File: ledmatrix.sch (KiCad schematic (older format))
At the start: 4 parts

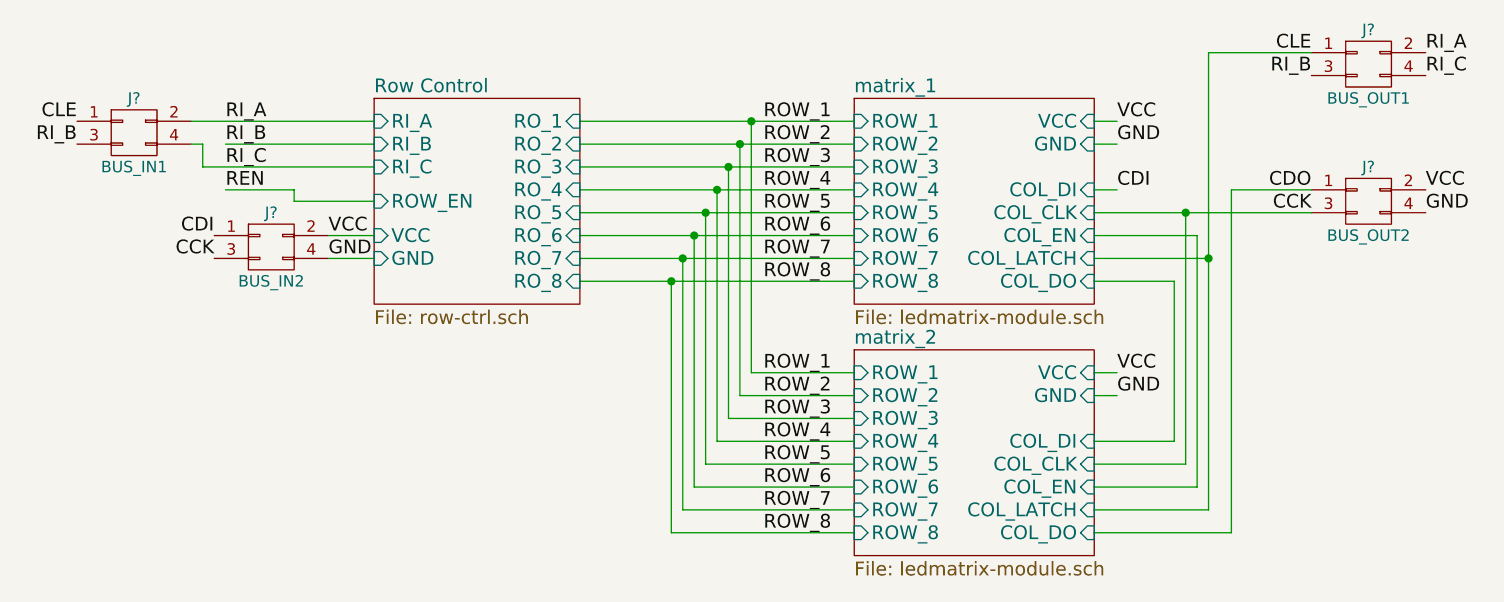
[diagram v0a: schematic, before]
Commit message: fix matrix module order
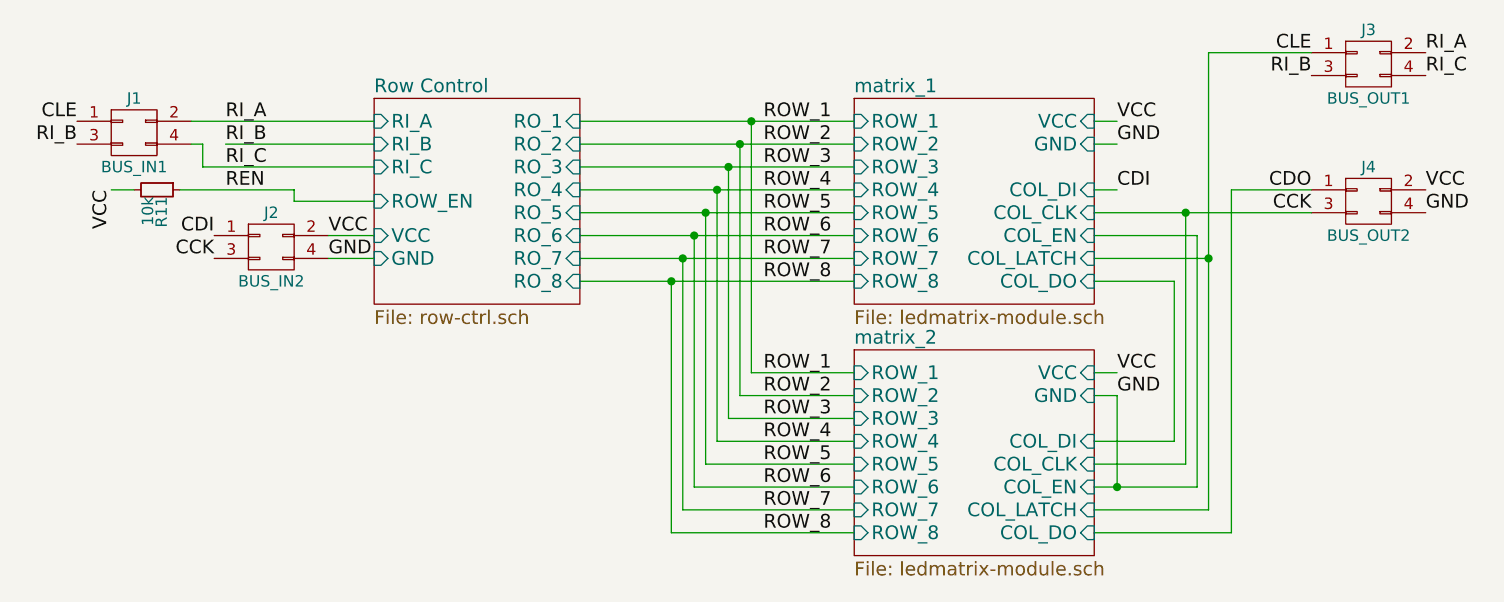
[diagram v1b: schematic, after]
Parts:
- added R11: 10k, symbol R_Small
- gave numbers to parts that had none: 4
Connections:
- net REN: now also R11.1
- net VCC: now also R11.2
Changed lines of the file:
@@
 REN
 Wire Wire Line
-	2250 1800 2550 1800
+	2050 1800 2550 1800
 Wire Wire Line
 	2550 1800 2550 1850
@@
 	6450 3000 6450 1900
 $Comp
-L CONN_02X02 J?
+L CONN_02X02 J4
 U 1 1 59AB19E8
 P 7250 1850
-F 0 "J?" H 7250 2000 50  0000 C CNN
+F 0 "J4" H 7250 2000 50  0000 C CNN
 F 1 "BUS_OUT2" H 7250 1700 50  0000 C CNN
 F 2 "" H 7250 650 50  0001 C CNN
@@
 	6500 2000 6050 2000
 $Comp
-L CONN_02X02 J?
+L CONN_02X02 J3
 U 1 1 59AB23F4
 P 7250 1250
-F 0 "J?" H 7250 1400 50  0000 C CNN
+F 0 "J3" H 7250 1400 50  0000 C CNN
 F 1 "BUS_OUT1" H 7250 1100 50  0000 C CNN
 F 2 "" H 7250 50  50  0001 C CNN
@@
 CLE
 $Comp
-L CONN_02X02 J?
+L CONN_02X02 J2
 U 1 1 59AB4B91
 P 2450 2050
-F 0 "J?" H 2450 2200 50  0000 C CNN
+F 0 "J2" H 2450 2200 50  0000 C CNN
 F 1 "BUS_IN2" H 2450 1900 50  0000 C CNN
 F 2 "" H 2450 850 50  0001 C CNN
@@
 $EndComp
 $Comp
-L CONN_02X02 J?
+L CONN_02X02 J1
 U 1 1 59AB4B97
 P 1850 1550
-F 0 "J?" H 1850 1700 50  0000 C CNN
+F 0 "J1" H 1850 1700 50  0000 C CNN
 F 1 "BUS_IN1" H 1850 1400 50  0000 C CNN
 F 2 "" H 1850 350 50  0001 C CNN
@@
 Wire Wire Line
 	2100 1500 2900 1500
+Wire Wire Line
+	6150 2700 6150 3100
+Connection ~ 6150 3100
+$Comp
+L R_Small R11
+U 1 1 59AB4113
+P 1950 1800
+F 0 "R11" H 1980 1820 50  0000 L CNN
+F 1 "10k" H 1980 1760 50  0000 L CNN
+F 2 "" H 1950 1800 50  0001 C CNN
+F 3 "" H 1950 1800 50  0001 C CNN
+	1    1950 1800
+	0    1    1    0
+$EndComp
+Wire Wire Line
+	1850 1800 1750 1800
+Text Label 1750 1800 3    60   ~ 0
+VCC
 $EndSCHEMATC

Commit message: save schematic changes
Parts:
- J1, J2: footprint (none) -> footprints:PINHDR_2x2_angled_male
- J3, J4: footprint (none) -> footprints:PINHDR_2x2_angled_female
- R11: footprint (none) -> footprints:0603_HAND
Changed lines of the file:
@@
 F 0 "J4" H 7250 2000 50  0000 C CNN
 F 1 "BUS_OUT2" H 7250 1700 50  0000 C CNN
-F 2 "" H 7250 650 50  0001 C CNN
+F 2 "footprints:PINHDR_2x2_angled_female" H 7250 650 50  0001 C CNN
 F 3 "" H 7250 650 50  0001 C CNN
 	1    7250 1850
@@
 F 0 "J3" H 7250 1400 50  0000 C CNN
 F 1 "BUS_OUT1" H 7250 1100 50  0000 C CNN
-F 2 "" H 7250 50  50  0001 C CNN
+F 2 "footprints:PINHDR_2x2_angled_female" H 7250 50  50  0001 C CNN
 F 3 "" H 7250 50  50  0001 C CNN
 	1    7250 1250
@@
 F 0 "J2" H 2450 2200 50  0000 C CNN
 F 1 "BUS_IN2" H 2450 1900 50  0000 C CNN
-F 2 "" H 2450 850 50  0001 C CNN
+F 2 "footprints:PINHDR_2x2_angled_male" H 2450 850 50  0001 C CNN
 F 3 "" H 2450 850 50  0001 C CNN
 	1    2450 2050
@@
 F 0 "J1" H 1850 1700 50  0000 C CNN
 F 1 "BUS_IN1" H 1850 1400 50  0000 C CNN
-F 2 "" H 1850 350 50  0001 C CNN
+F 2 "footprints:PINHDR_2x2_angled_male" H 1850 350 50  0001 C CNN
 F 3 "" H 1850 350 50  0001 C CNN
 	1    1850 1550
@@
 F 0 "R11" H 1980 1820 50  0000 L CNN
 F 1 "10k" H 1980 1760 50  0000 L CNN
-F 2 "" H 1950 1800 50  0001 C CNN
+F 2 "footprints:0603_HAND" H 1950 1800 50  0001 C CNN
 F 3 "" H 1950 1800 50  0001 C CNN
 	1    1950 1800

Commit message: add bypassing to schematic
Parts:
- added C1: 10u, footprints:0805_HAND, symbol C_Small
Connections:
- net GND: now also C1.2
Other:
- moved on the sheet: J2
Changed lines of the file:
@@
 Text Label 1600 1600 2    60   ~ 0
 RI_B
-Text Label 2200 2100 2    60   ~ 0
+Text Label 1650 2400 2    60   ~ 0
 CCK
 Text Label 1600 1500 2    60   ~ 0
@@
 L CONN_02X02 J2
 U 1 1 59AB4B91
-P 2450 2050
-F 0 "J2" H 2450 2200 50  0000 C CNN
-F 1 "BUS_IN2" H 2450 1900 50  0000 C CNN
-F 2 "footprints:PINHDR_2x2_angled_male" H 2450 850 50  0001 C CNN
-F 3 "" H 2450 850 50  0001 C CNN
-	1    2450 2050
+P 1900 2350
+F 0 "J2" H 1900 2500 50  0000 C CNN
+F 1 "BUS_IN2" H 1900 2200 50  0000 C CNN
+F 2 "footprints:PINHDR_2x2_angled_male" H 1900 1150 50  0001 C CNN
+F 3 "" H 1900 1150 50  0001 C CNN
+	1    1900 2350
 	1    0    0    -1
 $EndComp
@@
 VCC
 Wire Wire Line
-	2700 2000 2900 2000
+	2150 2000 2900 2000
 Wire Wire Line
 	2700 2100 2900 2100
-Text Label 2200 2000 2    60   ~ 0
+Text Label 1650 2300 2    60   ~ 0
 CDI
 Wire Wire Line
@@
 Text Label 1750 1800 3    60   ~ 0
 VCC
+Wire Wire Line
+	2150 2300 2150 2000
+$Comp
+L C_Small C1
+U 1 1 59ABF7FF
+P 2400 2100
+F 0 "C1" H 2410 2170 50  0000 L CNN
+F 1 "10u" H 2410 2020 50  0000 L CNN
+F 2 "footprints:0805_HAND" H 2400 2100 50  0001 C CNN
+F 3 "" H 2400 2100 50  0001 C CNN
+	1    2400 2100
+	1    0    0    -1
+$EndComp
+Wire Wire Line
+	2400 2200 2400 2400
+Wire Wire Line
+	2400 2400 2150 2400
+Text Label 2150 2400 0    60   ~ 0
+GND
 $EndSCHEMATC

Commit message: fully connected PCB
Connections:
- net VCC: now also C1.1
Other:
- moved on the sheet: C1
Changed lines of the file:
@@
 VCC
-Wire Wire Line
-	2150 2000 2900 2000
 Wire Wire Line
 	2700 2100 2900 2100
@@
 Wire Wire Line
 	2150 2300 2150 2000
-$Comp
-L C_Small C1
-U 1 1 59ABF7FF
-P 2400 2100
-F 0 "C1" H 2410 2170 50  0000 L CNN
-F 1 "10u" H 2410 2020 50  0000 L CNN
-F 2 "footprints:0805_HAND" H 2400 2100 50  0001 C CNN
-F 3 "" H 2400 2100 50  0001 C CNN
-	1    2400 2100
-	1    0    0    -1
-$EndComp
-Wire Wire Line
-	2400 2200 2400 2400
 Wire Wire Line
 	2400 2400 2150 2400
 Text Label 2150 2400 0    60   ~ 0
 GND
+$Comp
+L C_Small C1
+U 1 1 59ABF7FF
+P 2400 2150
+F 0 "C1" H 2410 2220 50  0000 L CNN
+F 1 "10u" H 2410 2070 50  0000 L CNN
+F 2 "footprints:0805_HAND" H 2400 2150 50  0001 C CNN
+F 3 "" H 2400 2150 50  0001 C CNN
+	1    2400 2150
+	1    0    0    -1
+$EndComp
+Wire Wire Line
+	2150 2000 2900 2000
+Connection ~ 2400 2000
+Wire Wire Line
+	2400 2050 2400 2000
+Wire Wire Line
+	2400 2250 2400 2400
 $EndSCHEMATC
